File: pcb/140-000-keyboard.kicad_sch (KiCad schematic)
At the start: 0 parts

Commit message: add keyboard
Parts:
- added C10, C9: 12p, symbol Device:C_Small
- added C11, C8: 1u, symbol Device:C
- added C6, C7: C, symbol Device:C
- added R15: 10k, symbol Device:R
- added R16, R17: 22, symbol Device:R
- added SW42: SW_Push, Kahil Switches:SW_Kailh_Choc_Mini_2.25u, symbol Switch:SW_Push
- added U3: ATmega32U4-A, Package_QFP:TQFP-44_10x10mm_P0.8mm, symbol MCU_Microchip_ATmega:ATmega32U4-A
- added Y1: 16MHz, symbol Device:Crystal_GND24_Small
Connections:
- new net: C6.2, C7.2, C8.2, R15.1, U3.14 (VCC), U3.2 (UVCC), U3.24 (AVCC), U3.34 (VCC), U3.44 (AVCC)
- new net: R15.2, SW42.2, U3.13 (~{RESET})
- new net: C10.2, U3.16 (XTAL2), Y1.1
- new net: C9.2, U3.17 (XTAL1), Y1.3
- new net: R16.2, U3.4 (D+)
- new net: R17.2, U3.3 (D-)
- new net: C11.1, U3.6 (UCAP)
- new net 141-000 Switch Matrix/COLUMN 1: U3.8 (PB0)
- new net 141-000 Switch Matrix/COLUMN 10: U3.32 (PC7)
- new net 141-000 Switch Matrix/COLUMN 11: U3.18 (PD0)
- new net 141-000 Switch Matrix/COLUMN 12: U3.19 (PD1)
- new net 141-000 Switch Matrix/COLUMN 13: U3.20 (PD2)
- new net 141-000 Switch Matrix/COLUMN 14: U3.21 (PD3)
- new net 141-000 Switch Matrix/COLUMN 2: U3.9 (PB1)
- new net 141-000 Switch Matrix/COLUMN 3: U3.10 (PB2)
- new net 141-000 Switch Matrix/COLUMN 4: U3.11 (PB3)
- new net 141-000 Switch Matrix/COLUMN 5: U3.28 (PB4)
- new net 141-000 Switch Matrix/COLUMN 6: U3.29 (PB5)
- new net 141-000 Switch Matrix/COLUMN 7: U3.30 (PB6)
- new net 141-000 Switch Matrix/COLUMN 8: U3.12 (PB7)
- new net 141-000 Switch Matrix/COLUMN 9: U3.31 (PC6)
- new net 141-000 Switch Matrix/ROW 1: U3.25 (PD4)
- new net 141-000 Switch Matrix/ROW 2: U3.22 (PD5)
- new net 141-000 Switch Matrix/ROW 3: U3.26 (PD6)
- new net 141-000 Switch Matrix/ROW 4: U3.27 (PD7)
- new net 141-000 Switch Matrix/ROW 5: U3.1 (PE6)
- new net GND: C10.1, C11.2, C6.1, C7.1, C8.1, C9.1, SW42.1, U3.15 (GND), U3.23 (GND), U3.35 (GND), U3.43 (GND), U3.5 (UGND), Y1.2 (G), Y1.4 (G)
- new net KEY_D+: R16.1
- new net KEY_D-: R17.1
- no-connect marks 0 -> 2
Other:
- added sheet 141-000 Switch Matrix (141-000-switch-matrix.kicad_sch)

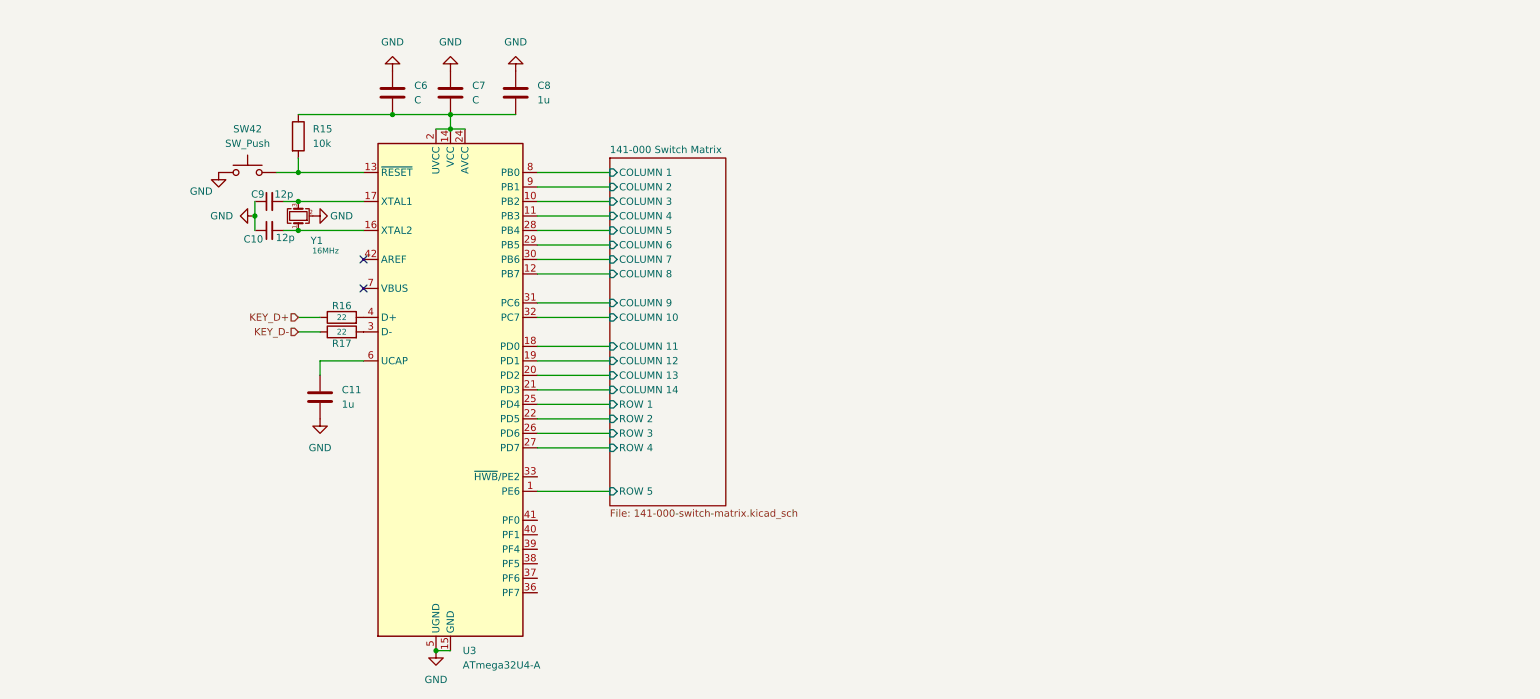
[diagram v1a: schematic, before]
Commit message: add rp2040 datasheet, and add rp2040 to keyboard unconnected
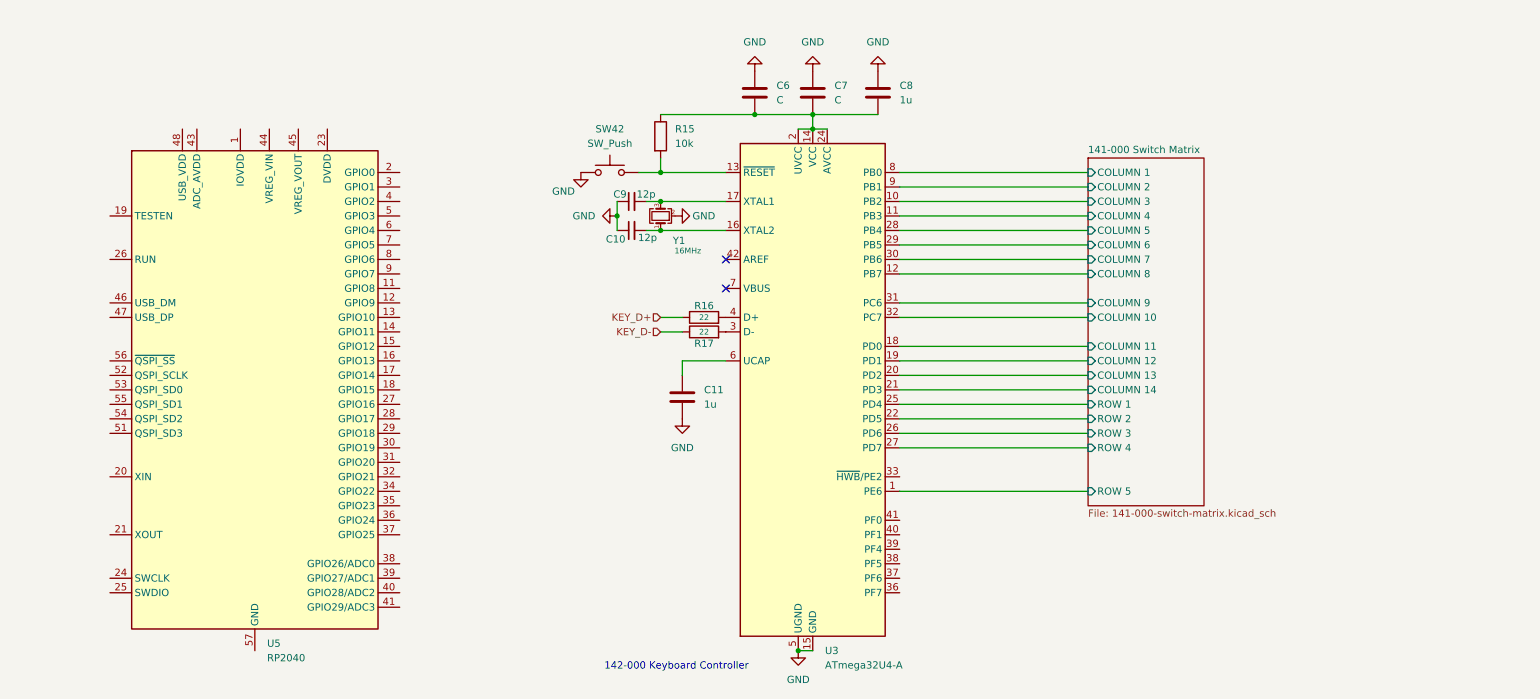
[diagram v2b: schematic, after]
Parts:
- added U5: RP2040, Package_DFN_QFN:QFN-56-1EP_7x7mm_P0.4mm_EP3.2x3.2mm, symbol MCU_RaspberryPi:RP2040
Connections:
- new net: U5.1 (IOVDD), U5.10 (IOVDD), U5.22 (IOVDD), U5.33 (IOVDD), U5.42 (IOVDD), U5.49 (IOVDD)
- new net: U5.23 (DVDD), U5.50 (DVDD)
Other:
- note added: "142-000 Keyboard Controller"
- moved on the sheet: C10, C11, C6, C7, C8, C9, R15, R16, R17, SW42, U3, Y1

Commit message: add git ignore, and new sheets etc
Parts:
- removed C10, C9: 12p, symbol Device:C_Small
- removed R17: 22, symbol Device:R
- removed SW42: SW_Push, Kahil Switches:SW_Kailh_Choc_Mini_2.25u, symbol Switch:SW_Push
- removed U3: ATmega32U4-A, Package_QFP:TQFP-44_10x10mm_P0.8mm, symbol MCU_Microchip_ATmega:ATmega32U4-A
- added C10, C12, C13, C14, C17, C18, C19, C9: 100n, symbol Device:C
- added C15, C16: 1u, symbol Device:C
- added C20, C21: 15p, symbol Device:C_Small
- added J2: Conn_01x02, symbol Connector_Generic:Conn_01x02
- added R17: 1k, symbol Device:R_Small
- added R18, R19: 27, symbol Device:R
- added U3: NCP1117-3.3_SOT223, Package_TO_SOT_SMD:SOT-223-3_TabPin2, symbol Regulator_Linear:NCP1117-3.3_SOT223
- added U6: W25Q16JVSS, Package_SO:SOIC-8_5.3x5.3mm_P1.27mm, symbol Memory_Flash:W25Q16JVSS
- C11, C8: value 1u -> 100n
- C6, C7: value C -> 10u
- R15: value 10k -> DNF (10k)
- R16: value 22 -> 1k
- Y1: value 16MHz -> ABM8-272-T3; footprint (none) -> perpetusest-parts:ABM8-272-T3_ABR
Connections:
- net 141-000 Switch Matrix/COLUMN 1: now also U5.2 (GPIO0)
- net 141-000 Switch Matrix/COLUMN 10: now also U5.12 (GPIO9)
- net 141-000 Switch Matrix/COLUMN 11: now also U5.13 (GPIO10)
- net 141-000 Switch Matrix/COLUMN 12: now also U5.14 (GPIO11)
- net 141-000 Switch Matrix/COLUMN 13: now also U5.15 (GPIO12)
- net 141-000 Switch Matrix/COLUMN 14: now also U5.16 (GPIO13)
- net 141-000 Switch Matrix/COLUMN 2: now also U5.3 (GPIO1)
- net 141-000 Switch Matrix/COLUMN 3: now also U5.4 (GPIO2)
- net 141-000 Switch Matrix/COLUMN 4: now also U5.5 (GPIO3)
- net 141-000 Switch Matrix/COLUMN 5: now also U5.6 (GPIO4)
- net 141-000 Switch Matrix/COLUMN 6: now also U5.7 (GPIO5)
- net 141-000 Switch Matrix/COLUMN 7: now also U5.8 (GPIO6)
- net 141-000 Switch Matrix/COLUMN 8: now also U5.9 (GPIO7)
- net 141-000 Switch Matrix/COLUMN 9: now also U5.11 (GPIO8)
- net 141-000 Switch Matrix/ROW 1: now also U5.17 (GPIO14)
- net 141-000 Switch Matrix/ROW 2: now also U5.18 (GPIO15)
- net 141-000 Switch Matrix/ROW 3: now also U5.27 (GPIO16)
- net 141-000 Switch Matrix/ROW 4: now also U5.28 (GPIO17)
- net 141-000 Switch Matrix/ROW 5: now also U5.29 (GPIO18)
- net GND: now also C6.2, C7.2, C8.2, U5.19 (TESTEN), U5.57 (GND), C10.2, C12.2, C13.2, C14.2, C15.2, C16.2, C19.2, C20.1, C21.2, C9.2, J2.1 (Pin_1), U3.1 (GND), U6.4 (GND); no longer C6.1, C7.1, C8.1
- net QSPI_CS: now reaches R15.2
- net QSPI_CS: now also R16.2, U5.56 (~{QSPI_SS}), U6.1 (~{CS})
- net at Y1.1: now also C21.1, R17.1
- net at Y1.3: now also U5.20 (XIN), C20.2
- net +3.3V: now reaches U5.1 (IOVDD), U5.10 (IOVDD), U5.22 (IOVDD), U5.33 (IOVDD), U5.42 (IOVDD), U5.49 (IOVDD)
- net +3.3V: now also C11.1, C7.1, C8.1, R15.1, U5.43 (ADC_AVDD), U5.44 (VREG_VIN), U5.48 (USB_VDD), C10.1, C12.1, C13.1, C14.1, C15.1, C19.1, C9.1, U3.2 (VO), U6.8 (VCC)
- net at U5.21 (XOUT): now also R17.2
- net +1V1: now reaches U5.23 (DVDD), U5.50 (DVDD)
- net +1V1: now also U5.45 (VREG_VOUT), C16.1, C17.1, C18.1
- net 2040_SWCLK: now reaches U5.24 (SWCLK)
- net 2040_SWDIO: now reaches U5.25 (SWDIO)
- net at U5.46 (USB_DM): now also R18.1
- net at U5.47 (USB_DP): now also R19.2
- net QSPI_SD3: now reaches U5.51 (QSPI_SD3)
- net QSPI_SD3: now also U6.7 (~{HOLD}/~{RESET}/IO_{3})
- net QSPI_SCLK: now reaches U5.52 (QSPI_SCLK)
- net QSPI_SCLK: now also U6.6 (CLK)
- net QSPI_SD0: now reaches U5.53 (QSPI_SD0)
- net QSPI_SD0: now also U6.5 (DI/IO_{0})
- net QSPI_SD2: now reaches U5.54 (QSPI_SD2)
- net QSPI_SD2: now also U6.3 (~{WP}/IO_{2})
- net QSPI_SD1: now reaches U5.55 (QSPI_SD1)
- net QSPI_SD1: now also U6.2 (DO/IO_{1})
- net KEY_D+ renamed ~{USB_BOOT}
- net ~{USB_BOOT}: now also J2.2 (Pin_2)
- new net: C17.2, C18.2
- new net +5V: C6.1, U3.3 (VI)
- new net 2040_USB_D+: R19.1
- new net 2040_USB_D-: R18.2
- no-connect marks 2 -> 11
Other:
- note added: "Ensure C15 is close to pin 44"
- note added: "Ensure C16 is close to pin 45"
- note added: "Spi Flash"
- note added: "connect this jumper to go into usb boot mode"
- note added: "usb data traces should be routed at 90 Ohm characteristic impedance"
- moved on the sheet: U5

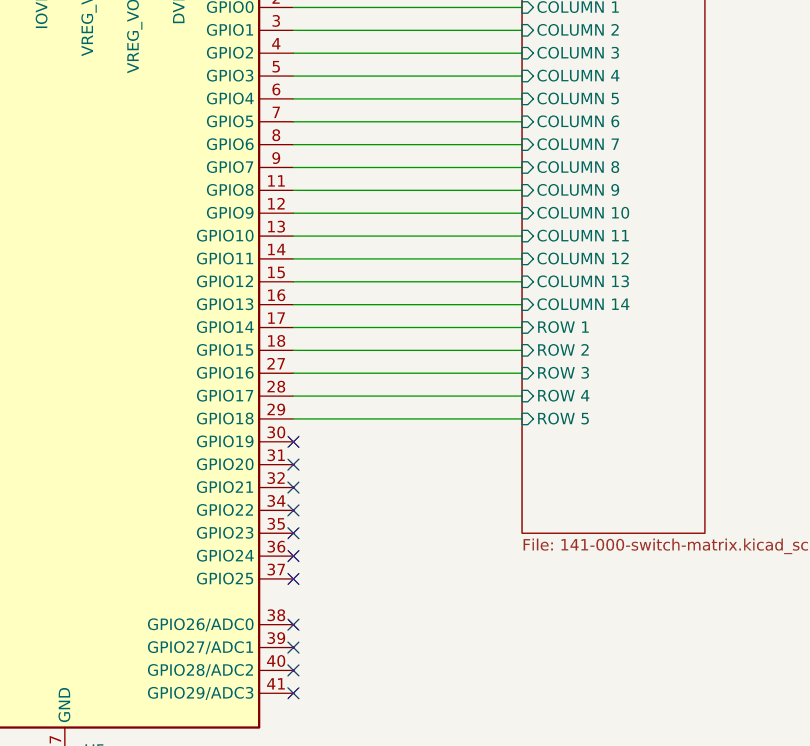
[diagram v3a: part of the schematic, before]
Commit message: major keyboard components completed
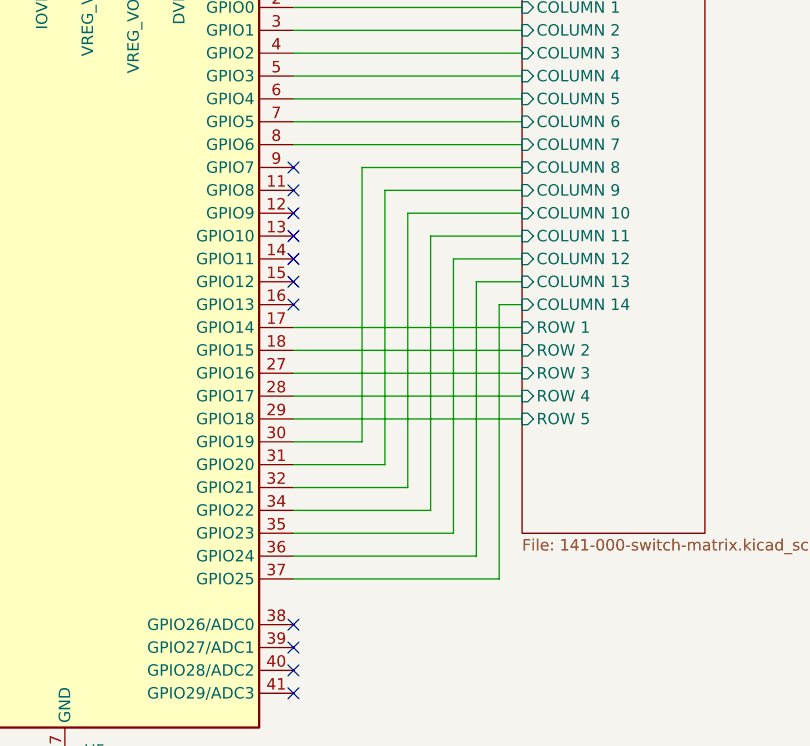
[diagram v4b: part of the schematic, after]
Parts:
- C10, C11, C12, C13, C14, C15, C16, C17, C18, C19, C20, C21, C6, C7, C8, C9: footprint (none) -> Capacitor_SMD:C_0402_1005Metric
- R15, R16, R17, R18, R19: footprint (none) -> Resistor_SMD:R_0402_1005Metric
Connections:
- net 141-000 Switch Matrix/COLUMN 10: now also U5.32 (GPIO21); no longer U5.12 (GPIO9)
- net 141-000 Switch Matrix/COLUMN 11: now also U5.34 (GPIO22); no longer U5.13 (GPIO10)
- net 141-000 Switch Matrix/COLUMN 12: now also U5.35 (GPIO23); no longer U5.14 (GPIO11)
- net 141-000 Switch Matrix/COLUMN 13: now also U5.36 (GPIO24); no longer U5.15 (GPIO12)
- net 141-000 Switch Matrix/COLUMN 14: now also U5.37 (GPIO25); no longer U5.16 (GPIO13)
- net 141-000 Switch Matrix/COLUMN 8: now also U5.30 (GPIO19); no longer U5.9 (GPIO7)
- net 141-000 Switch Matrix/COLUMN 9: now also U5.31 (GPIO20); no longer U5.11 (GPIO8)
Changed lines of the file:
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@@
 	)
 	(no_connect
-		(at 222.25 107.95)
+		(at 222.25 69.85)
 	)
 	(no_connect
-		(at 222.25 102.87)
+		(at 222.25 115.57)
 	)
 	(no_connect
-		(at 222.25 105.41)
+		(at 222.25 74.93)
 	)
 	(no_connect
-		(at 222.25 115.57)
+		(at 222.25 64.77)
 	)
 	(no_connect
@@
 	)
 	(no_connect
-		(at 222.25 118.11)
+		(at 222.25 62.23)
 	)
 	(no_connect
-		(at 222.25 92.71)
+		(at 222.25 118.11)
 	)
 	(no_connect
-		(at 222.25 97.79)
+		(at 222.25 113.03)
 	)
 	(no_connect
-		(at 222.25 113.03)
+		(at 222.25 67.31)
 	)
 	(no_connect
-		(at 222.25 95.25)
+		(at 222.25 77.47)
 	)
 	(no_connect
-		(at 222.25 100.33)
+		(at 222.25 72.39)
 	)
 	(wire
 		(pts
-			(xy 222.25 77.47) (xy 247.65 77.47)
+			(xy 237.49 69.85) (xy 237.49 100.33)
 		)
 		(stroke
@@
 	(wire
 		(pts
-			(xy 184.15 36.83) (xy 186.69 36.83)
+			(xy 237.49 100.33) (xy 222.25 100.33)
 		)
 		(stroke
@@
 	(wire
 		(pts
-			(xy 96.52 107.95) (xy 96.52 104.14)
+			(xy 184.15 36.83) (xy 186.69 36.83)
 		)
 		(stroke
@@
 	(wire
 		(pts
-			(xy 222.25 69.85) (xy 247.65 69.85)
+			(xy 96.52 107.95) (xy 96.52 104.14)
 		)
 		(stroke
@@
 	(wire
 		(pts
-			(xy 222.25 72.39) (xy 247.65 72.39)
+			(xy 240.03 102.87) (xy 222.25 102.87)
+		)
+		(stroke
+			(width 0)
+			(type default)
+		)
+	)
+	(wire
+		(pts
+			(xy 247.65 64.77) (xy 232.41 64.77)
 		)
 		(stroke
@@
 	(wire
 		(pts
+			(xy 247.65 72.39) (xy 240.03 72.39)
+		)
+		(stroke
+			(width 0)
+			(type default)
+		)
+	)
+	(wire
+		(pts
 			(xy 222.25 59.69) (xy 247.65 59.69)
 		)
@@
 	(wire
 		(pts
+			(xy 229.87 62.23) (xy 229.87 92.71)
+		)
+		(stroke
+			(width 0)
+			(type default)
+		)
+	)
+	(wire
+		(pts
+			(xy 240.03 72.39) (xy 240.03 102.87)
+		)
+		(stroke
+			(width 0)
+			(type default)
+		)
+	)
+	(wire
+		(pts
 			(xy 171.45 100.33) (xy 154.94 100.33)
 		)
@@
 	(wire
 		(pts
+			(xy 234.95 67.31) (xy 247.65 67.31)
+		)
+		(stroke
+			(width 0)
+			(type default)
+		)
+	)
+	(wire
+		(pts
 			(xy 149.86 30.48) (xy 156.21 30.48)
 		)
@@
 	(wire
 		(pts
+			(xy 247.65 69.85) (xy 237.49 69.85)
+		)
+		(stroke
+			(width 0)
+			(type default)
+		)
+	)
+	(wire
+		(pts
 			(xy 184.15 22.86) (xy 184.15 27.94)
 		)
@@
 	(wire
 		(pts
+			(xy 234.95 67.31) (xy 234.95 97.79)
+		)
+		(stroke
+			(width 0)
+			(type default)
+		)
+	)
+	(wire
+		(pts
 			(xy 43.18 60.96) (xy 44.45 60.96)
 		)
@@
 	(wire
 		(pts
-			(xy 222.25 64.77) (xy 247.65 64.77)
+			(xy 242.57 105.41) (xy 222.25 105.41)
 		)
 		(stroke
@@
 	(wire
 		(pts
+			(xy 247.65 77.47) (xy 245.11 77.47)
+		)
+		(stroke
+			(width 0)
+			(type default)
+		)
+	)
+	(wire
+		(pts
 			(xy 228.6 30.48) (xy 238.76 30.48)
 		)
@@
 	(wire
 		(pts
-			(xy 222.25 62.23) (xy 247.65 62.23)
+			(xy 245.11 77.47) (xy 245.11 107.95)
+		)
+		(stroke
+			(width 0)
+			(type default)
+		)
+	)
+	(wire
+		(pts
+			(xy 247.65 62.23) (xy 229.87 62.23)
 		)
 		(stroke
@@
 	(wire
 		(pts
-			(xy 222.25 74.93) (xy 247.65 74.93)
+			(xy 228.6 22.86) (xy 238.76 22.86)
 		)
 		(stroke
@@
 	(wire
 		(pts
-			(xy 228.6 22.86) (xy 238.76 22.86)
+			(xy 232.41 64.77) (xy 232.41 95.25)
 		)
 		(stroke
@@
 	(wire
 		(pts
+			(xy 229.87 92.71) (xy 222.25 92.71)
+		)
+		(stroke
+			(width 0)
+			(type default)
+		)
+	)
+	(wire
+		(pts
 			(xy 55.88 105.41) (xy 55.88 107.95)
 		)
@@
 	(wire
 		(pts
-			(xy 146.05 105.41) (xy 154.94 105.41)
+			(xy 247.65 74.93) (xy 242.57 74.93)
 		)
 		(stroke
@@
 	(wire
 		(pts
-			(xy 222.25 67.31) (xy 247.65 67.31)
+			(xy 146.05 105.41) (xy 154.94 105.41)
 		)
 		(stroke
@@
 	(wire
 		(pts
+			(xy 234.95 97.79) (xy 222.25 97.79)
+		)
+		(stroke
+			(width 0)
+			(type default)
+		)
+	)
+	(wire
+		(pts
 			(xy 222.25 90.17) (xy 247.65 90.17)
 		)
@@
 	(wire
 		(pts
+			(xy 232.41 95.25) (xy 222.25 95.25)
+		)
+		(stroke
+			(width 0)
+			(type default)
+		)
+	)
+	(wire
+		(pts
 			(xy 222.25 80.01) (xy 247.65 80.01)
 		)
@@
 		)
 	)
+	(wire
+		(pts
+			(xy 245.11 107.95) (xy 222.25 107.95)
+		)
+		(stroke
+			(width 0)
+			(type default)
+		)
+	)
+	(wire
+		(pts
+			(xy 242.57 74.93) (xy 242.57 105.41)
+		)
+		(stroke
+			(width 0)
+			(type default)
+		)
+	)
 	(label "QSPI_CS"
 		(at 171.45 77.47 180)
@@
 			)
 		)
-		(property "Footprint" ""
+		(property "Footprint" "Capacitor_SMD:C_0402_1005Metric"
 			(at 229.5652 30.48 0)
 			(effects
@@
 			)
 		)
-		(property "Footprint" ""
+		(property "Footprint" "Capacitor_SMD:C_0402_1005Metric"
 			(at 157.1752 30.48 0)
 			(effects
@@
 			)
 		)
-		(property "Footprint" ""
+		(property "Footprint" "Resistor_SMD:R_0402_1005Metric"
 			(at 165.1 71.628 90)
 			(effects
@@
 			)
 		)
-		(property "Footprint" ""
+		(property "Footprint" "Capacitor_SMD:C_0402_1005Metric"
 			(at 216.8652 35.56 0)
 			(effects
@@
 			)
 		)
-		(property "Footprint" ""
+		(property "Footprint" "Capacitor_SMD:C_0402_1005Metric"
 			(at 178.7652 35.56 0)
 			(effects
@@
 			)
 		)
-		(property "Footprint" ""
+		(property "Footprint" "Capacitor_SMD:C_0402_1005Metric"
 			(at 138.1252 30.48 0)
 			(effects
@@
 			)
 		)
-		(property "Footprint" ""
+		(property "Footprint" "Capacitor_SMD:C_0402_1005Metric"
 			(at 143.51 100.33 0)
 			(effects
@@
 			)
 		)
-		(property "Footprint" ""
+		(property "Footprint" "Resistor_SMD:R_0402_1005Metric"
 			(at 166.37 105.41 0)
 			(effects
@@
 			)
 		)
-		(property "Footprint" ""
+		(property "Footprint" "Capacitor_SMD:C_0402_1005Metric"
 			(at 143.51 105.41 0)
 			(effects
@@
 			)
 		)
-		(property "Footprint" ""
+		(property "Footprint" "Capacitor_SMD:C_0402_1005Metric"
 			(at 150.8252 30.48 0)
 			(effects
@@
 			)
 		)
-		(property "Footprint" ""
+		(property "Footprint" "Capacitor_SMD:C_0402_1005Metric"
 			(at 119.0752 30.48 0)
 			(effects
@@
 			)
 		)
-		(property "Footprint" ""
+		(property "Footprint" "Capacitor_SMD:C_0402_1005Metric"
 			(at 92.4052 115.57 0)
 			(effects
@@
 			)
 		)
-		(property "Footprint" ""
+		(property "Footprint" "Capacitor_SMD:C_0402_1005Metric"
 			(at 144.4752 30.48 0)
 			(effects
@@
 			)
 		)
-		(property "Footprint" ""
+		(property "Footprint" "Capacitor_SMD:C_0402_1005Metric"
 			(at 131.7752 30.48 0)
 			(effects
@@
 			)
 		)
-		(property "Footprint" ""
+		(property "Footprint" "Resistor_SMD:R_0402_1005Metric"
 			(at 165.1 65.532 90)
 			(effects
@@
 			)
 		)
-		(property "Footprint" ""
+		(property "Footprint" "Capacitor_SMD:C_0402_1005Metric"
 			(at 60.6552 115.57 0)
 			(effects
@@
 			)
 		)
-		(property "Footprint" ""
+		(property "Footprint" "Resistor_SMD:R_0402_1005Metric"
 			(at 57.15 60.198 90)
 			(effects
@@
 			)
 		)
-		(property "Footprint" ""
+		(property "Footprint" "Capacitor_SMD:C_0402_1005Metric"
 			(at 91.1352 44.45 0)
 			(effects
@@
 			)
 		)
-		(property "Footprint" ""
+		(property "Footprint" "Capacitor_SMD:C_0402_1005Metric"
 			(at 239.7252 30.48 0)
 			(effects
@@
 			)
 		)
-		(property "Footprint" ""
+		(property "Footprint" "Resistor_SMD:R_0402_1005Metric"
 			(at 69.342 48.26 90)
 			(effects
@@
 			)
 		)
-		(property "Footprint" ""
+		(property "Footprint" "Capacitor_SMD:C_0402_1005Metric"
 			(at 125.4252 30.48 0)
 			(effects
